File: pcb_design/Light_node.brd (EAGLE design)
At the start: 38 parts, among them U10 MCP73831T-2ACI/OT, U20 LIS3DHTR, U30 ATmega328P, U40 MIC5225-3.3v, U50 COMMON_ANODE_DIODE, Y30 12MHz

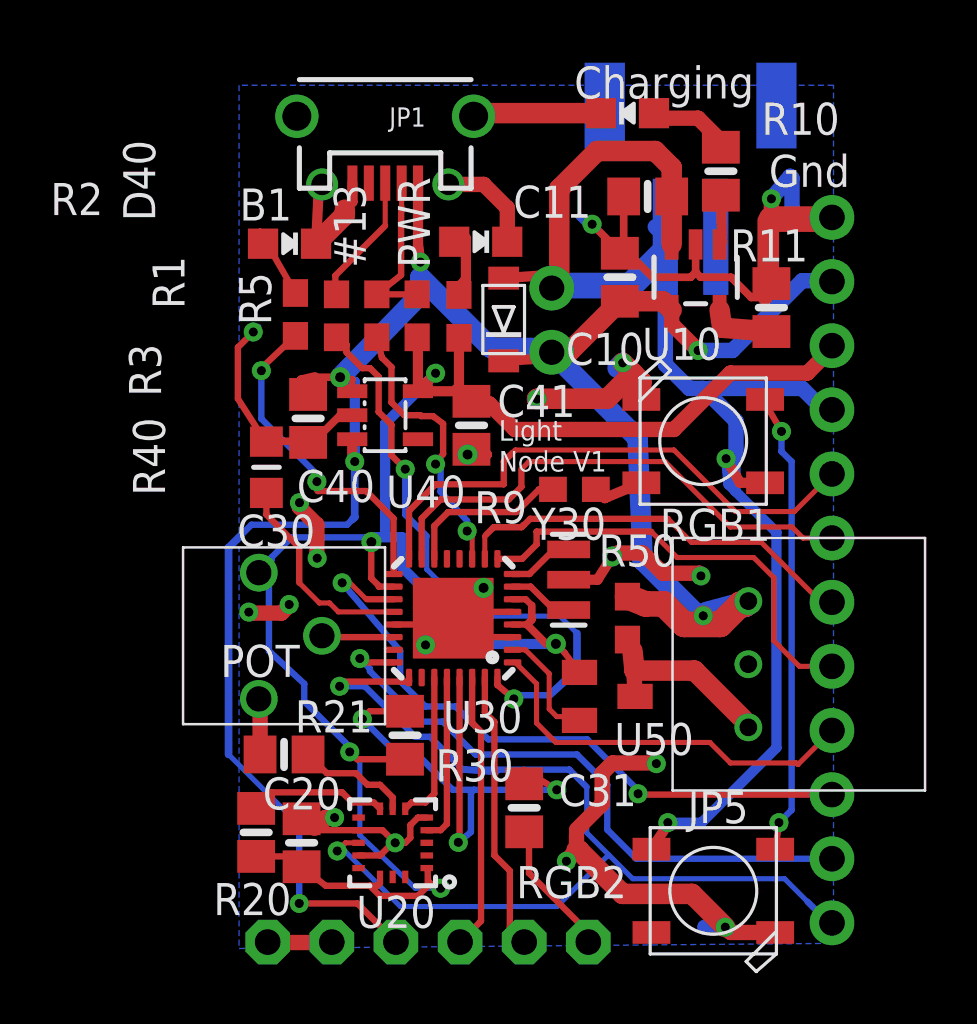
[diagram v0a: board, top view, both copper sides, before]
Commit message: added the switch to the bottom
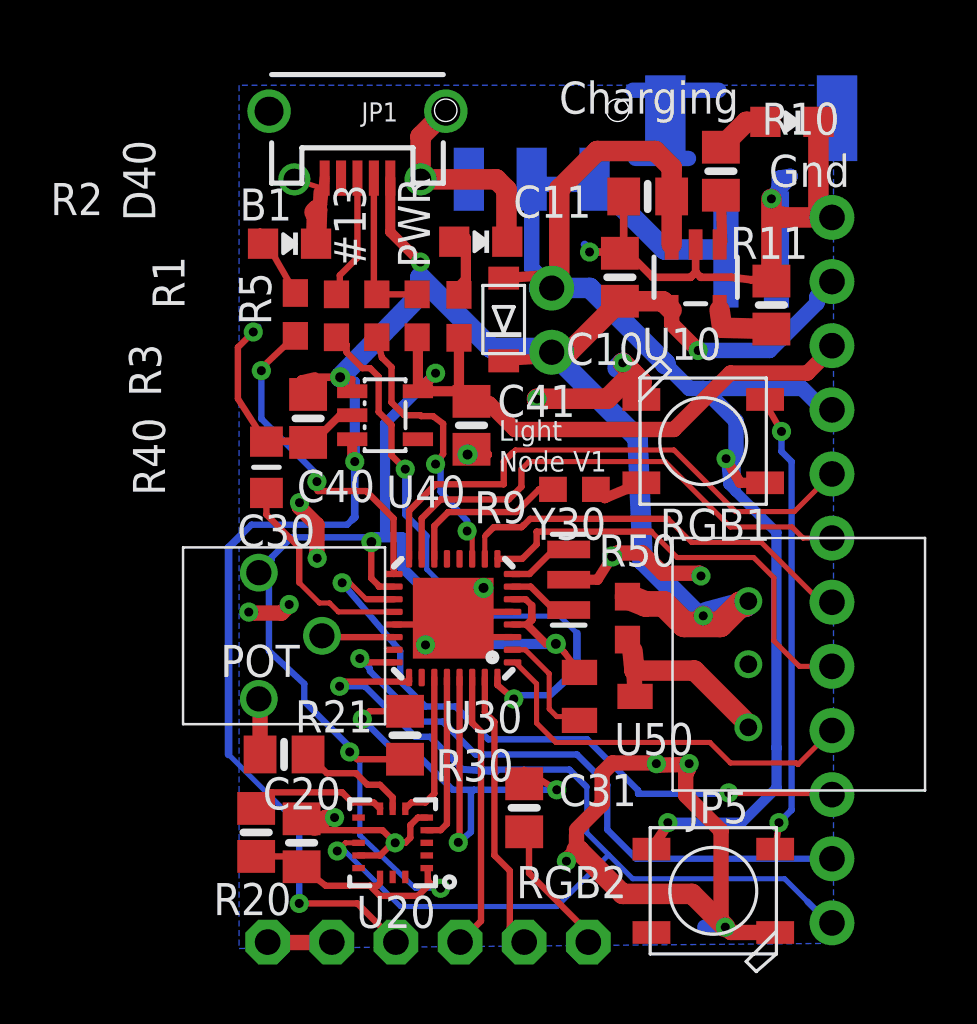
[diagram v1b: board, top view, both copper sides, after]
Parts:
- added U$8: SPDT_NO_GNDSMT, 0_Shibbs1:JS102011SAQN
- moved CH_LED 6.52 mm to (22.9, 34.0), turned to 270 degrees
- moved JP3 2.45 mm to (21.3, 32.6)
- moved JP1 1.12 mm to (5.70, 34.4)
- moved R11 0.10 mm to (22.1, 26.7)
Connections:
- net VBAT: now also U$8.P$1, U$8.P$2
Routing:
- net GND: track 107.3 -> 127.8 mm, vias 19 -> 20
- net VBAT: track 60.4 -> 69.0 mm
- net N$9: track 3.36 -> 2.18 mm
